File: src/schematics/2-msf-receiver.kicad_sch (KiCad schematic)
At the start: 75 parts, among them U201 TPS7A2040PDQNR, U202 TPS7A2036PDBVR, U203 MCP6499, U204 MCP6499, U205 74HC595BQ

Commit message: Added part numbers for the resistors.
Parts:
- R201, R202, R208, R220, R221: Manufacturer (none) -> Yageo; Manufacturer2 (none) -> Vishay; Manufacturer2PartNumber (none) -> MCS04020D4991BE000; ManufacturerPartNumber (none) -> RT0402BRD074K99L
- R203, R209: Manufacturer (none) -> Yageo; Manufacturer2 (none) -> Walsin; Manufacturer2PartNumber (none) -> WR04X000PTL; ManufacturerPartNumber (none) -> RC0402FR-070RL
- R205, R211: Manufacturer (none) -> TE Connectivity; ManufacturerPartNumber (none) -> CPF0402B27RE1
- R206, R207: Manufacturer (none) -> Yageo; Manufacturer2 (none) -> Panasonic; Manufacturer2PartNumber (none) -> ERA-2AEB432X; ManufacturerPartNumber (none) -> RT0402BRD074K3L
- R212, R213, R215, R216, R217, R218: Manufacturer (none) -> Yageo; Manufacturer2 (none) -> Panasonic; Manufacturer2PartNumber (none) -> ERA-2AEB2491X; ManufacturerPartNumber (none) -> RT0402BRD072K49L
- R214, R219: Manufacturer (none) -> Yageo; Manufacturer2 (none) -> Panasonic; Manufacturer2PartNumber (none) -> ERA-2AEB680X; ManufacturerPartNumber (none) -> RT0402BRD0768RL
- R222, R223, R224: Manufacturer (none) -> Walsin; Manufacturer2 (none) -> Yageo; Manufacturer2PartNumber (none) -> RC0402FR-0733KL; ManufacturerPartNumber (none) -> WR04X3302FTL

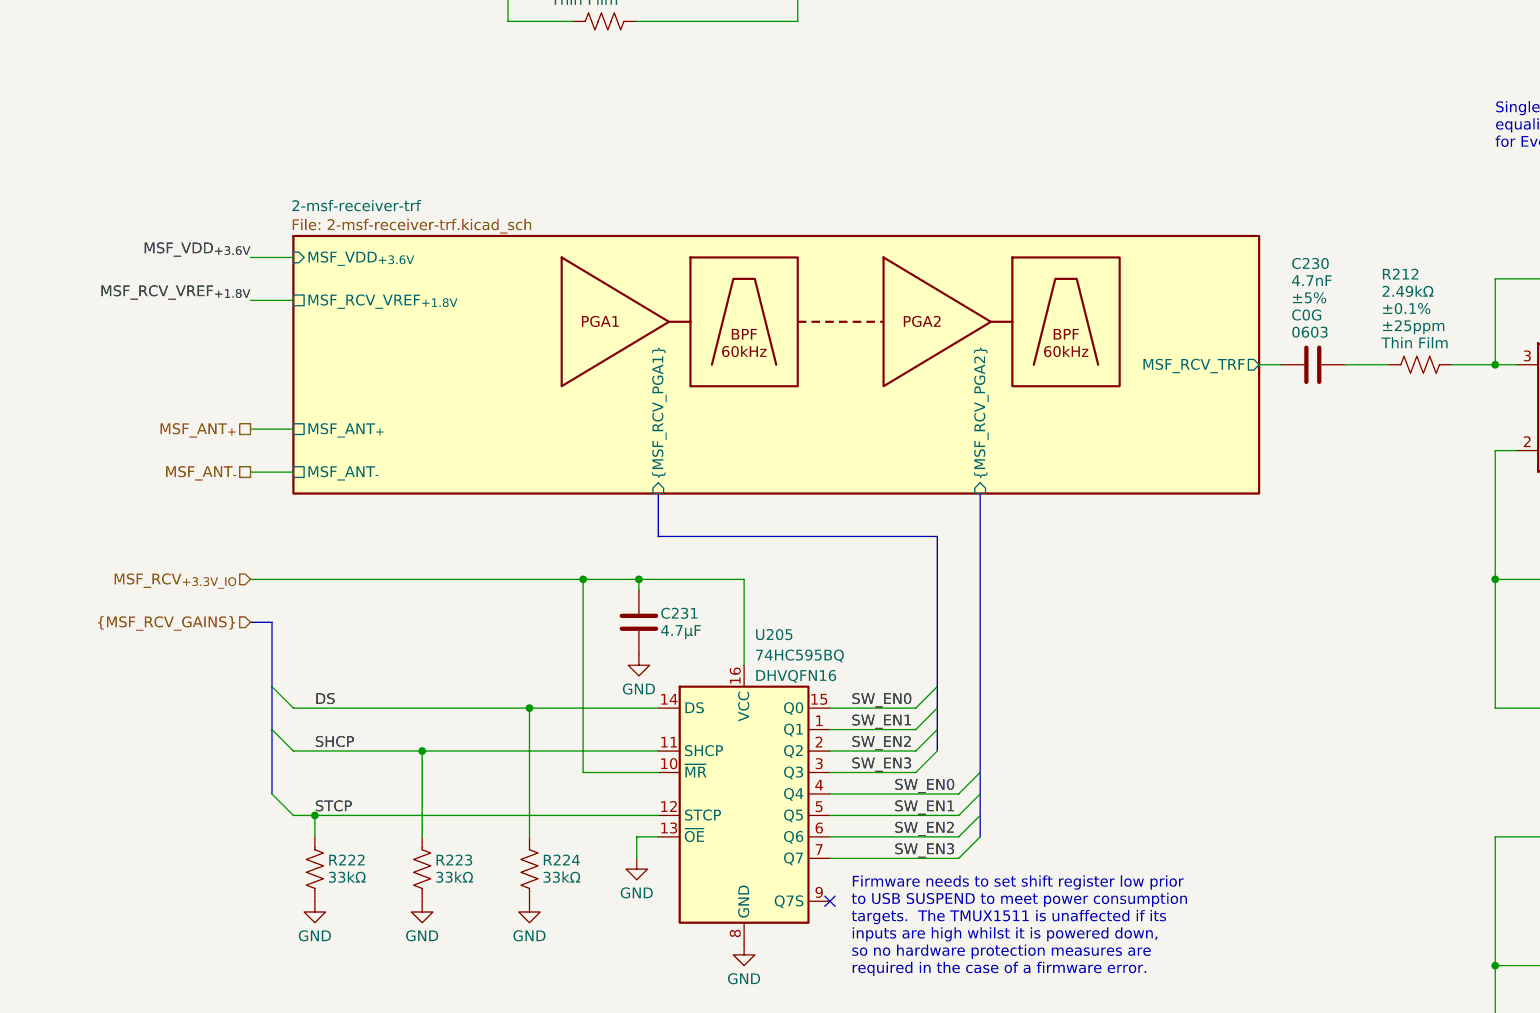
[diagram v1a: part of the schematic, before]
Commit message: Clean up the remaining ERC flags.
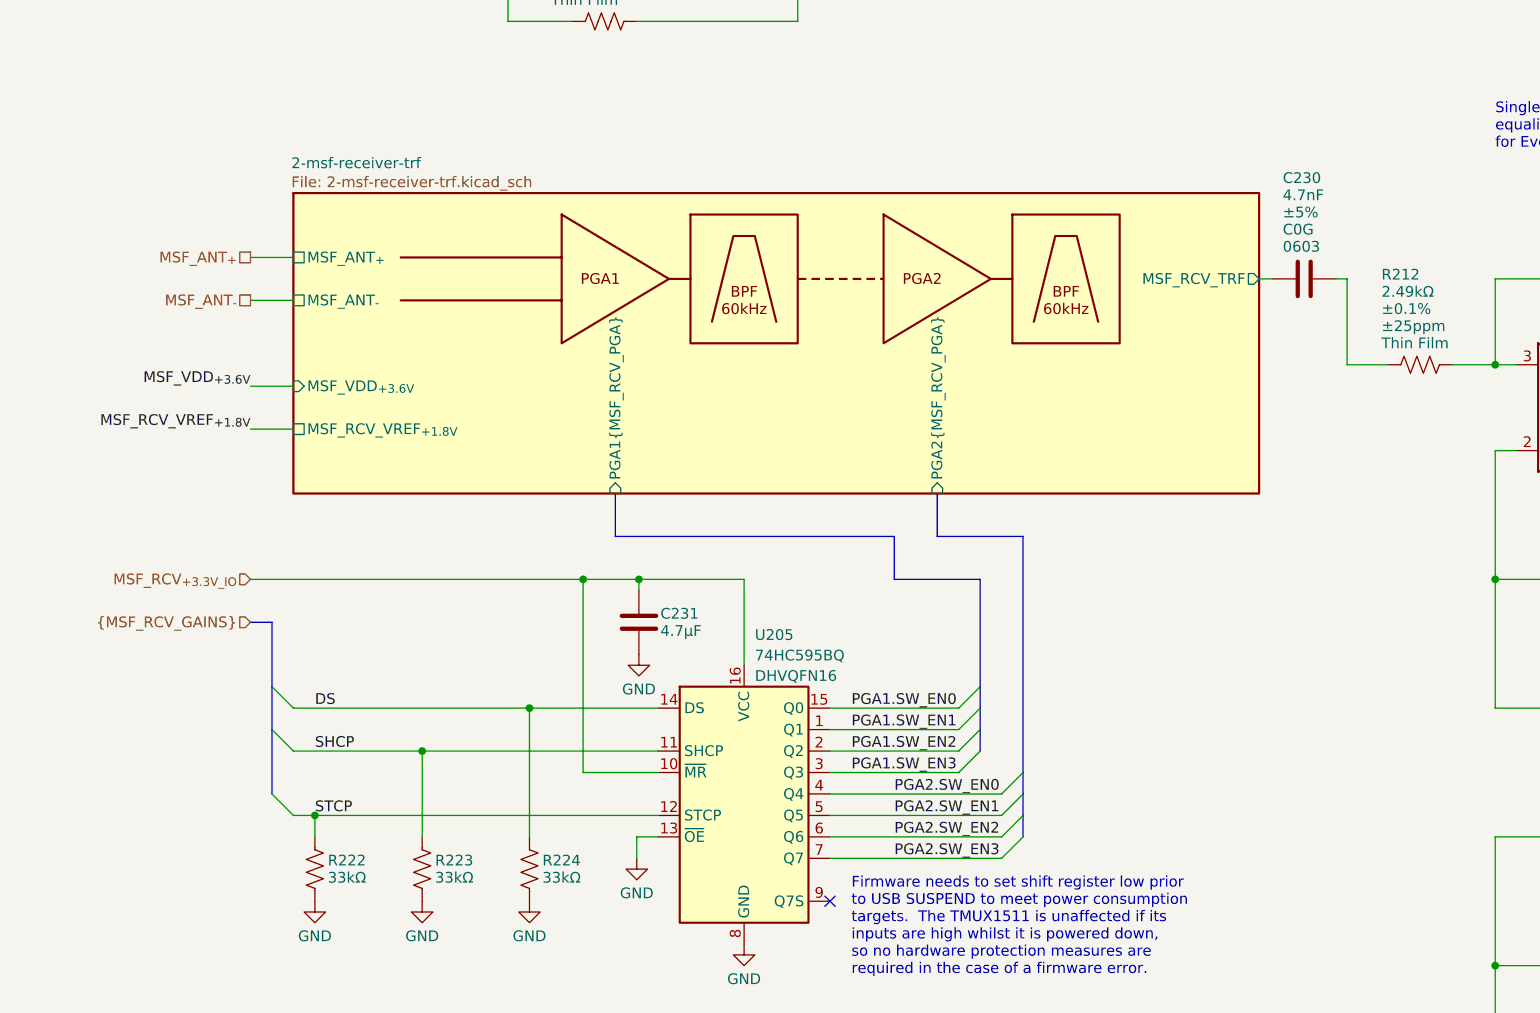
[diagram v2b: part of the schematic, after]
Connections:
- net GND renamed GND_PWRIN
- net SW_EN0 renamed PGA1.SW_EN0
- net PGA1.SW_EN0: no longer U205.4 (Q4)
- net SW_EN1 renamed PGA1.SW_EN1
- net PGA1.SW_EN1: no longer U205.5 (Q5)
- net SW_EN2 renamed PGA1.SW_EN2
- net PGA1.SW_EN2: no longer U205.6 (Q6)
- net SW_EN3 renamed PGA1.SW_EN3
- net PGA1.SW_EN3: no longer U205.7 (Q7)
- new net PGA2.SW_EN0: U205.4 (Q4)
- new net PGA2.SW_EN1: U205.5 (Q5)
- new net PGA2.SW_EN2: U205.6 (Q6)
- new net PGA2.SW_EN3: U205.7 (Q7)
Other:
- sheet 2-msf-receiver-trf ports: added PGA1{MSF_RCV_PGA}, PGA2{MSF_RCV_PGA}; removed {MSF_RCV_PGA1}, {MSF_RCV_PGA2}
- moved on the sheet: C230

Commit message: Some footprint / net bugfixes identified whilst generating the initial PCB.
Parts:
- D201, D202, D203, D204, D205, D206: footprint restall-generic-sot:SOD-323 -> restall-generic-sot:SOD323
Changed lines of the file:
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@@
       (effects (font (size 1.27 1.27)) (justify left))
     )
-    (property "Footprint" "restall-generic-sot:SOD-323" (at 273.05 87.63 0)
+    (property "Footprint" "restall-generic-sot:SOD323" (at 273.05 87.63 0)
       (effects (font (size 1.27 1.27)) (justify right) hide)
     )
@@
       (effects (font (size 1.27 1.27)) (justify left))
     )
-    (property "Footprint" "restall-generic-sot:SOD-323" (at 374.65 92.71 0)
+    (property "Footprint" "restall-generic-sot:SOD323" (at 374.65 92.71 0)
       (effects (font (size 1.27 1.27)) (justify right) hide)
     )
@@
       (effects (font (size 1.27 1.27)) (justify left))
     )
-    (property "Footprint" "restall-generic-sot:SOD-323" (at 49.53 87.63 0)
+    (property "Footprint" "restall-generic-sot:SOD323" (at 49.53 87.63 0)
       (effects (font (size 1.27 1.27)) (justify right) hide)
     )
@@
       (effects (font (size 1.27 1.27)) (justify left))
     )
-    (property "Footprint" "restall-generic-sot:SOD-323" (at 163.83 104.14 0)
+    (property "Footprint" "restall-generic-sot:SOD323" (at 163.83 104.14 0)
       (effects (font (size 1.27 1.27)) (justify right) hide)
     )
@@
       (effects (font (size 1.27 1.27)) (justify left))
     )
-    (property "Footprint" "restall-generic-sot:SOD-323" (at 166.37 260.35 0)
+    (property "Footprint" "restall-generic-sot:SOD323" (at 166.37 260.35 0)
       (effects (font (size 1.27 1.27)) (justify right) hide)
     )
@@
       (effects (font (size 1.27 1.27)) (justify left))
     )
-    (property "Footprint" "restall-generic-sot:SOD-323" (at 163.83 92.71 0)
+    (property "Footprint" "restall-generic-sot:SOD323" (at 163.83 92.71 0)
       (effects (font (size 1.27 1.27)) (justify right) hide)
     )

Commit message: Started to lay out the PCB.
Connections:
- net GND_PWRIN renamed GND

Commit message: PCB routing.
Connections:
- net MSF_OUT_{+} renamed MSF_OUT+
- net MSF_OUT_{-} renamed MSF_OUT-
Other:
- note added: "Route as length-matched differential pair, ideally with Z_{odd}=68Ω but this is not critical because transmission line effects will not be present. Unfortunately the JLCPCB stack-up only lets us approach Z_{even}=103Ω (Z_{odd}=51.5Ω), about 25% less than our target. ADC V_{fs}≃±2.5V_{p-p}-7% headroom ADC V_{cm}≃1.25V Under fault conditions or transients it is possible to see nearly 3.7V from the 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"
- note removed: "Route as length-matched differential lines, Z_{0}=68Ω ADC V_{fs}≃±2.5V_{p-p}-7% headroom ADC V_{cm}≃1.25V Under fault conditions or transients it is possible to see nearly 3.7V from the op-amp on the ADC pins. With a worst-case MCU V_{DD} of around 3.1V, there could be an excess 0.6V injecting current into the ESD protection diodes. The PIC32 datasheet states that the maximum injection current is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"
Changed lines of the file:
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@@
     (effects (font (size 1.27 1.27)) (justify left bottom))
   )
-  (text "Route as length-matched\ndifferential lines, Z_{0}=68Ω\n\nADC V_{fs}≃±2.5V_{p-p}-7% headroom\nADC V_{cm}≃1.25V\n\nUnder fault conditions or transients it is possible to see nearly 3.7V\nfrom the op-amp on the ADC pins.  With a worst-case MCU V_{DD} of\naround 3.1V, there could be an excess 0.6V injecting current into the\nESD protection diodes.  The PIC32 datasheet states that the maximum\ninjection current is ±15mA; the 68Ω series resistors should limit\nthis to less than 9mA.  Schottky diodes could have been used at the\nexpense of offsets caused by reverse leakage currents and the distortion\nintroduced by further mismatch of the differential inputs."
-    (at 246.38 233.68 0)
+  (text "Route as length-matched differential pair, ideally with Z_{odd}=68Ω but\nthis is not critical because transmission line effects will not be present.\n\nUnfortunately the JLCPCB stack-up only lets us approach Z_{even}=103Ω\n(Z_{odd}=51.5Ω), about 25% less than our target.\n\nADC V_{fs}≃±2.5V_{p-p}-7% headroom\nADC V_{cm}≃1.25V\n\nUnder fault conditions or transients it is possible to see nearly 3.7V\nfrom the op-amp on the ADC pins.  With a worst-case MCU V_{DD} of\naround 3.1V, there could be an excess 0.6V injecting current into the\nESD protection diodes.  The PIC32 datasheet states that the maximum\ninjection current is ±15mA; the 68Ω series resistors should limit\nthis to less than 9mA.  Schottky diodes could have been used at the\nexpense of offsets caused by reverse leakage currents and the distortion\nintroduced by further mismatch of the differential inputs."
+    (at 246.38 238.76 0)
     (effects (font (size 1.27 1.27)) (justify left bottom))
   )
@@
     (effects (font (size 1.27 1.27)) (justify right))
   )
-  (hierarchical_label "MSF_OUT_{+}" (shape output) (at 233.68 218.44 0) (fields_autoplaced)
+  (hierarchical_label "MSF_OUT+" (shape output) (at 233.68 218.44 0) (fields_autoplaced)
     (effects (font (size 1.27 1.27)) (justify left))
   )
@@
     (effects (font (size 1.27 1.27)) (justify left))
   )
-  (hierarchical_label "MSF_OUT_{-}" (shape output) (at 233.68 223.52 0) (fields_autoplaced)
+  (hierarchical_label "MSF_OUT-" (shape output) (at 233.68 223.52 0) (fields_autoplaced)
     (effects (font (size 1.27 1.27)) (justify left))
   )

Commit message: PCB routing.
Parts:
- TP203, TP204: footprint restall-generic-test:testpoint-SP3050A-with-short-gnd -> restall-generic-test:th-testpoint-0.5mm-with-short-gnd
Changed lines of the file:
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@@
       (effects (font (size 1.27 1.27)) (justify right) hide)
     )
-    (property "Footprint" "restall-generic-test:testpoint-SP3050A-with-short-gnd" (at 127 92.71 0)
+    (property "Footprint" "restall-generic-test:th-testpoint-0.5mm-with-short-gnd" (at 127 92.71 0)
       (effects (font (size 1.27 1.27)) (justify right) hide)
     )
@@
       (effects (font (size 1.27 1.27)) (justify right) hide)
     )
-    (property "Footprint" "restall-generic-test:testpoint-SP3050A-with-short-gnd" (at 337.82 92.71 0)
-      (effects (font (size 1.27 1.27)) (justify right) hide)
-    )
+    (property "Footprint" "restall-generic-test:th-testpoint-0.5mm-with-short-gnd" (at 337.82 92.71 0)
+      (effects (font (size 1.27 1.27)) (justify right) hide)
+    )

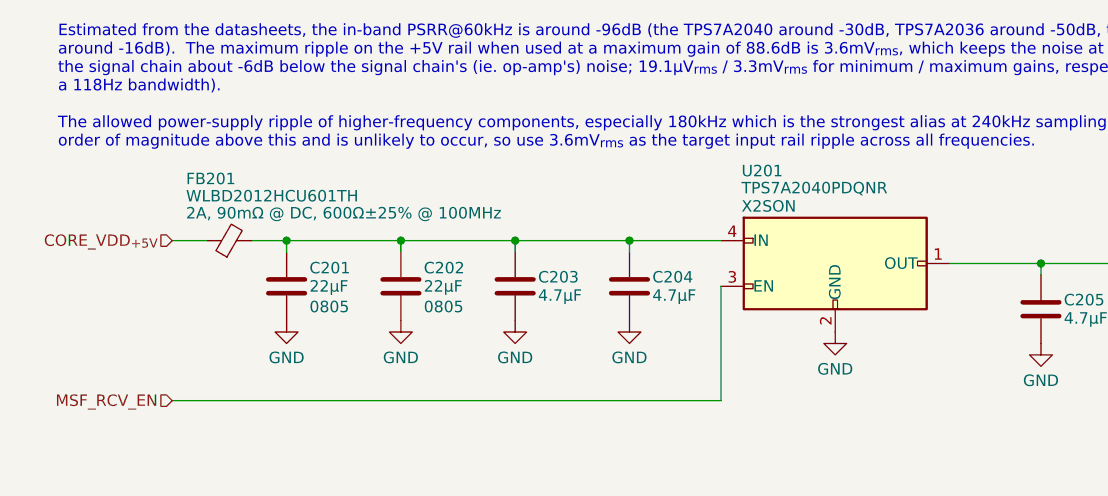
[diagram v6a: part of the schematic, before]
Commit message: PCB routing.  Fixed most of the DRC violations.
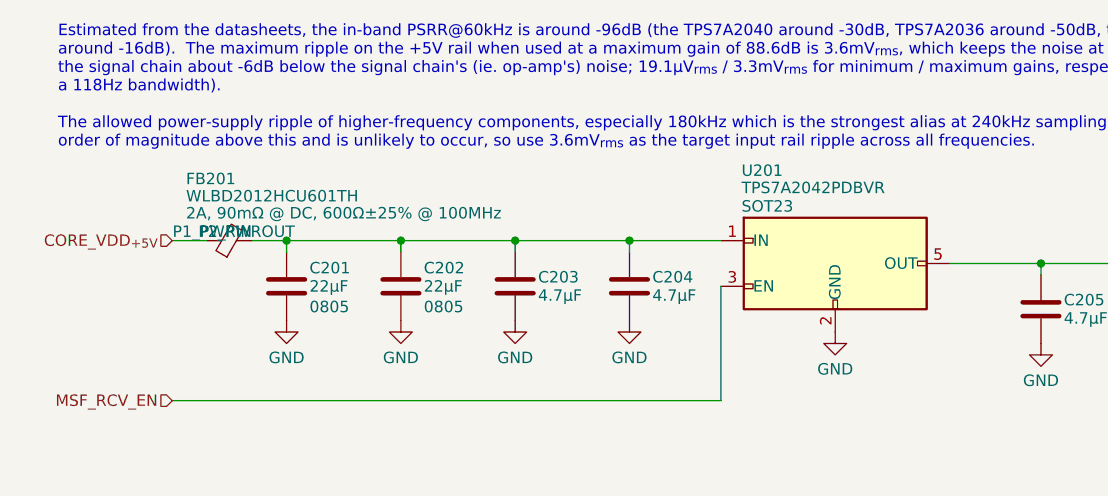
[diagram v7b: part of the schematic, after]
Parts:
- removed U201: TPS7A2040PDQNR, restall-manufacturer-ti:X2SON4-1x1mm-0.65mm-expad-0.48x0.48mm, symbol restall-manufacturer-ti:TPS7A20??PDQNR
- added U201: TPS7A2042PDBVR, restall-manufacturer-ti:TPS7A20??PDBVR, symbol restall-manufacturer-ti:TPS7A20??PDBVR
- TP201: footprint restall-generic-test:testpoint-SP3050A-with-short-gnd -> restall-generic-test:th-testpoint-0.5mm-with-short-gnd
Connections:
- net GND: now also U201.2 (GND)
- net MSF_RCV_EN: now also U201.3 (EN)
- net at C201.1, C202.1, C203.1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: now also U201.1 (IN)
- net at C205.1, C206.1, C207.1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: now also U201.5 (OUT)
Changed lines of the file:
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@@
+    )
+  )
+  (symbol (lib_id "restall-manufacturer-ti:TPS7A20??PDBVR") (at 104.14 43.18 0) (unit 1)
+    (in_bom yes) (on_board yes) (dnp no)
+    (property "Reference" "U201" (at 93.726 32.8594 0)
+      (effects (font (size 1.27 1.27)) (justify left))
+    )
+    (property "Value" "TPS7A2042PDBVR" (at 93.726 34.7756 0)
+      (effects (font (size 1.27 1.27)) (justify left))
+    )
+    (property "Footprint" "restall-manufacturer-ti:TPS7A20??PDBVR" (at 109.855 49.53 0)
+      (effects (font (size 1.27 1.27)) (justify left) hide)
+    )
+    (property "Datasheet" "https://www.ti.com/lit/ds/symlink/tps7a20.pdf" (at 109.855 51.435 0)
+      (effects (font (size 1.27 1.27)) (justify left) hide)
+    )
+    (property "Package" "SOT23" (at 93.726 36.83 0)
+      (effects (font (size 1.27 1.27)) (justify left))
+    )
+    (property "Manufacturer" "Texas Instruments" (at 117.348 32.766 0)
+      (effects (font (size 1.27 1.27)) (justify left) hide)
+    )
+    (property "ManufacturerPartNumber" "TPS7A2042PDBVR" (at 117.348 34.798 0)
+      (effects (font (size 1.27 1.27)) (justify left) hide)
+    )
+    (pin "4")
+    (pin "3")
+    (pin "5")
+    (pin "1")
+    (pin "2")
+    (instances
+      (project "msf-owl-clock"
+        (path "/56d623d3-22db-4d43-a9d9-e6bb4bb68946/ce863d79-d266-4984-b56b-ca957df41c84"
+          (reference "U201") (unit 1)
+        )
+      )
     )
   )
@@
       (effects (font (size 1.27 1.27)) (justify right) hide)
     )
-    (property "Footprint" "restall-generic-test:testpoint-SP3050A-with-short-gnd" (at 191.77 36.83 0)
+    (property "Footprint" "restall-generic-test:th-testpoint-0.5mm-with-short-gnd" (at 191.77 36.83 0)
       (effects (font (size 1.27 1.27)) (justify right) hide)
     )
@@
         )
       )
-    )
-  )
-  (symbol (lib_id "restall-manufacturer-ti:TPS7A20??PDQNR") (at 104.14 43.18 0) (unit 1)
-    (in_bom yes) (on_board yes) (dnp no)
-    (property "Reference" "U201" (at 93.726 32.9042 0)
-      (effects (font (size 1.27 1.27)) (justify left))
-    )
-    (property "Value" "TPS7A2040PDQNR" (at 93.726 34.798 0)
-      (effects (font (size 1.27 1.27)) (justify left))
-    )
-    (property "Footprint" "restall-manufacturer-ti:X2SON4-1x1mm-0.65mm-expad-0.48x0.48mm" (at 109.855 49.53 0)
-      (effects (font (size 1.27 1.27)) (justify left) hide)
-    )
-    (property "Datasheet" "https://www.ti.com/lit/ds/symlink/tps7a20.pdf" (at 109.855 51.435 0)
-      (effects (font (size 1.27 1.27)) (justify left) hide)
-    )
-    (property "Manufacturer" "Texas Instruments" (at 117.348 32.766 0)
-      (effects (font (size 1.27 1.27)) (justify left) hide)
-    )
-    (property "ManufacturerPartNumber" "TPS7A2040PDQNR" (at 117.348 34.798 0)
-      (effects (font (size 1.27 1.27)) (justify left) hide)
-    )
-    (property "Package" "X2SON" (at 93.726 36.83 0)
-      (effects (font (size 1.27 1.27)) (justify left))
-    )
-    (pin "5")
-    (pin "1")
-    (pin "2")
-    (pin "4")
-    (pin "3")
-    (instances
-      (project "msf-owl-clock"
-        (path "/56d623d3-22db-4d43-a9d9-e6bb4bb68946/ce863d79-d266-4984-b56b-ca957df41c84"
-          (reference "U201") (unit 1)
-        )
-      )

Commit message: Further tweaks, tidy-ups and silkscreen labelling.
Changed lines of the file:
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@@
   (title_block
     (title "MSF Owl Clock - MSF Receiver Module")
+    (date "June 2024")
     (rev "0.1")
     (company "Pete Restall <pete@restall.net>")
